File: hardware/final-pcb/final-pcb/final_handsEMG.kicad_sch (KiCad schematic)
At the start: 35 parts, among them J1 Conn_02x13_Odd_Even, U1 ADS1299CPAG

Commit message: finalpcb update (3.23.25)
schematic nearly done, need footprint assignments.
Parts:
- removed D2, D3, D4, D5, D6, D7: TPD4E1B06DRLR, DRL6_TEX, symbol TPD4E1B06DRLR:TPD4E1B06DRLR
- added C29, C31, C33, C37: 10uF, symbol Device:C_Small
- added C30: 0.01uF, symbol Device:C_Small
- added C32, C35, C36, C38, C39, C40: 2.2uF, symbol Device:C_Small
- added D2, D3, D4, D5, D6, D8: TPD4E1B06DCKR, DCK6_TEX, symbol TPD4E1B06DCKR:TPD4E1B06DCKR
- added D9: D_Small, symbol Device:D_Small
- added J2: Conn_01x02, symbol Connector_Generic:Conn_01x02
- added U2: STM32L496ZGT6, STM32L496ZGT6:QFP50P2200X2200X160-144N, symbol STM32L496ZGT6:STM32L496ZGT6
- added U3: LM2664M6/NOPB, DBV0006A_N, symbol LM2664M6/NOPB:LM2664M6_NOPB
- added U4: TLV70025QDDCRQ1, TLV70025QDDCRQ1:SOT95P280X110-5N, symbol TLV70025QDDCRQ1:TLV70025QDDCRQ1
- added U5: MCP1754T-3302E/OT, SOT-23-5_MC_MCH, symbol MCP1754T-3302E/OT:MCP1754T-3302E_OT
- added U6: TPS72325DBVR, TPS72325DBVR:SOT95P280X145-5N, symbol TPS72325DBVR:TPS72325DBVR
- added sC38, sC39, sC43, sC44, sC45, sC46, sC47, sC48, sC55, sC62, sC63, sC65, sC68, sC71: 100nF, symbol Device:C_Small
- added sC64: 1uF_X5R_0603, symbol Device:C_Small
- added sC66, sC69: 4.7uF_X54_0603, symbol Device:C_Small
- added sC67, sC70: 1uF, symbol Device:C_Polarized_Small
- added sC72: 4.7uF, symbol Device:C_Polarized_Small
- added sCN3: USB_B_Micro, symbol Connector:USB_B_Micro
- added sD4: ESDALC6V1_1U2, symbol Device:D_Small
- added sL2: FerriteBead_Small, symbol Device:FerriteBead_Small
- added sLD14: Red, symbol Device:D_Small
- added sLD15: Green, symbol Device:D_Small
- added sR18, sR19, sR9: 10K, symbol Device:R_Small
- added sR21, sR23: 47K, symbol Device:R_Small
- added sR22: 620, symbol Device:R_Small
- added sR24: 22K, symbol Device:R_Small
- added sR25: 330, symbol Device:R_Small
- added sT3: 9013, symbol Transistor_BJT:Q_NPN_BEC
- added sU10: USBLC6-2SC6, Package_TO_SOT_SMD:SOT-23-6, symbol Power_Protection:USBLC6-2SC6
- added sU14: STMPS2151STR, SOT23-5L_STM, symbol STMPS2151STR:STMPS2151STR
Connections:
- net 1N: now also D3.4 (IO3)
- net 1P: now also D2.1 (IO1)
- net 2N: now also D3.2 (IO2)
- net 2P: now also D3.5 (IO4)
- net 3N: now also D4.4 (IO3)
- net 3P: now also D3.1 (IO1)
- net 4N: now also D4.2 (IO2)
- net 4P: now also D4.5 (IO4)
- net 5N: now also D5.4 (IO3)
- net 5P: now also D4.1 (IO1)
- net 6N: now also D5.2 (IO2)
- net 6P: now also D5.5 (IO4)
- net 7N: now also D6.4 (IO3)
- net 7P: now also D5.1 (IO1)
- net 8N: now also D6.2 (IO2)
- net 8P: now also D6.5 (IO4)
- net BIAS: now also D8.4 (IO3)
- net GNDA: now also C29.2, C30.2, C32.2, C33.2, C35.2, C36.2, C37.2, C38.2, C39.2, C40.2, D2.3 (GND), D3.3 (GND), D4.3 (GND), D5.3 (GND), D6.3 (GND), D8.1 (IO1), D8.3 (GND), J2.1 (Pin_1), U2.30 (VSSA/VREF-), U2.31 (VREF-), U3.1 (GND), U4.2 (GND), U5.2 (GND), U6.1 (GND), sC67.2, sC68.2
- net SRB1: now also D2.5 (IO4)
- net SRB2: now also D2.2 (IO2)
- net AVDD renamed +2V5
- net +2V5: now also C35.1, C37.1, D8.2 (IO2), U2.32 (VREF+), U2.33 (VDDA), U4.5 (OUT), sC67.1, sC68.1, sC70.1, sC71.1, sL2.2
- net AVSS renamed -2V5
- net -2V5: now also C29.1, C32.1, D2.4 (IO3), U6.5 (OUT)
- net DVDD renamed +3V3
- net +3V3: now also C38.1, C40.1, U2.106 (VDDUSB), U2.108 (VDD__6), U2.121 (VDD__7), U2.131 (VDDIO2__1), U2.144 (VDD__8), U2.17 (VDD), U2.39 (VDD__1), U2.52 (VDD__2), U2.62 (VDD__3), U2.72 (VDD__4), U2.84 (VDD__5), U2.95 (VDDIO2), U3.4 (SD_N), U3.5 (V+), U4.1 (IN), U4.3 (EN), U5.5 (VOUT), sC38.1, sC39.1, sC43.1, sC44.1, sC45.1, sC46.1, sC47.1, sC48.1, sC55.1, sC62.1, sC63.1, sC64.1, sC65.1, sC66.1, sC69.1, sL2.1, sR21.2, sR22.2, sR25.2, sU14.5 (IN)
- new net: D9.2 (A), J2.2 (Pin_2)
- new net: sC70.2, sC71.2
- new net: sLD14.1 (K), sR21.1, sU14.3 (FAULT)
- new net: sLD14.2 (A), sR22.1
- new net: C30.1, U6.4 (NR)
- new net: U2.138 (PH3-BOOT0), sR9.1
- new net: sLD15.1 (K), sT3.3 (C)
- new net: sLD15.2 (A), sR25.1
- new net: sR23.1, sR24.2, sT3.1 (B)
- new net: sR19.1, sU14.4 (EN)
- new net: C31.1, U3.6 (OUT)
- new net: C31.2, U3.3 (CAP-)
- new net -RAW: C33.1, C36.1, U3.6 (OUT), U6.2 (IN), U6.3 (EN)
- new net 3V Enable: U5.3 (*SHDN)
- new net GND: U2.107 (VSS__7), U2.120 (VSS__8), U2.130 (VSS__9), U2.143 (VSS__10), U2.16 (VSS), U2.38 (VSS__1), U2.51 (VSS__2), U2.61 (VSS__3), U2.71 (VSS__4), U2.83 (VSS__5), U2.94 (VSS__6), sC38.2, sC39.2, sC43.2, sC44.2, sC45.2, sC46.2, sC47.2, sC48.2, sC55.2, sC62.2, sC63.2, sC64.2, sC65.2, sC66.2, sC69.2, sC72.2, sCN3.5 (GND), sD4.2 (A), sR19.2, sR24.1, sR9.2, sT3.2 (E), sU10.2 (GND), sU14.2 (GND)
- new net PA1: U2.35 (PA1)
- new net PA10: U2.102 (PA10), sCN3.4 (ID), sD4.1 (K)
- new net PA11: U2.103 (PA11), sCN3.2 (D-), sU10.3 (I/O2), sU10.4 (I/O2)
- new net PA12: U2.104 (PA12), sCN3.3 (D+), sU10.1 (I/O1), sU10.6 (I/O1)
- new net PA13: U2.105 (PA13(JTMS/SWDIO))
- new net PA14: U2.109 (PA14(JTCK/SWCLK))
- new net PA4: U2.40 (PA4)
- new net PA6: U2.42 (PA6)
- new net PA7: U2.43 (PA7)
- new net PA8: U2.100 (PA8)
- new net PA9: U2.101 (PA9), sR18.1
- new net PB12: U2.73 (PB12)
- new net PB13: U2.74 (PB13)
- new net PB14: U2.75 (PB14)
- new net PB15: U2.76 (PB15)
- new net PB3: U2.133 (PB3(JTDO/TRACESWO))
- new net PB7: U2.137 (PB7)
- new net PC13: U2.7 (PC13)
- new net PC7: U2.97 (PC7)
- new net PD10: U2.79 (PD10)
- new net PD11: U2.80 (PD11)
- new net PD12: U2.81 (PD12)
- new net PD13: U2.82 (PD13)
- new net PD8: U2.77 (PD8)
- new net PD9: U2.78 (PD9)
- new net PG13: U2.128 (PG13)
- new net PG14: U2.129 (PG14)
- new net RAW: C39.1, D9.1 (K), U5.1 (VIN)
- new net USB_VBUS: sC72.1, sCN3.1 (VBUS), sR18.2, sR23.2, sU10.5 (VBUS), sU14.1 (OUT)
- new net VBAT: U2.6 (VBAT)
- new net /NRST: U2.25 (~{NRST})
- no-connect marks 2 -> 91
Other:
- removed sheet FinalPCB_STM32
- moved on the sheet: C1, C11, C12, C13, C14, C15, C17, C18, C19, C2, C21, C22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

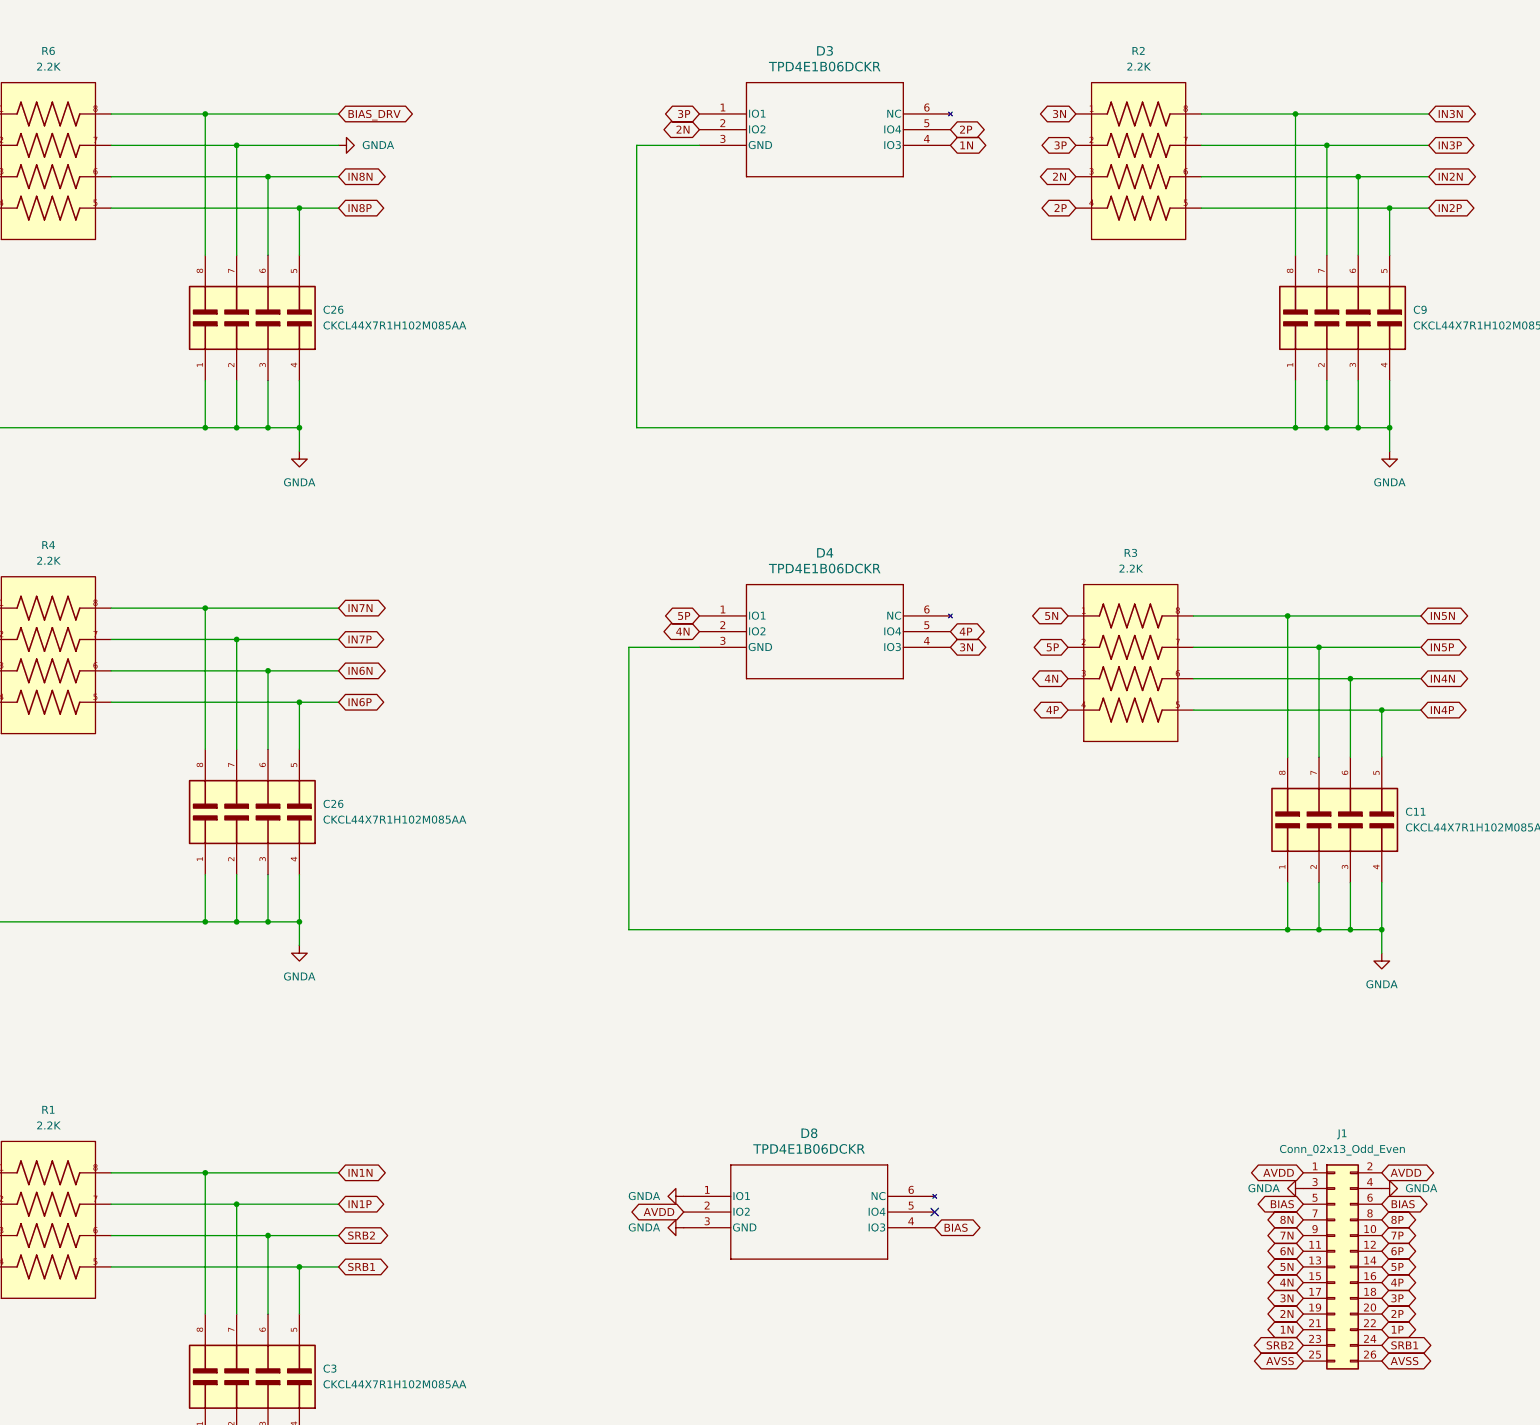
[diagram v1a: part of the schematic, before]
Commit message: half ads layout done (3.24.25)
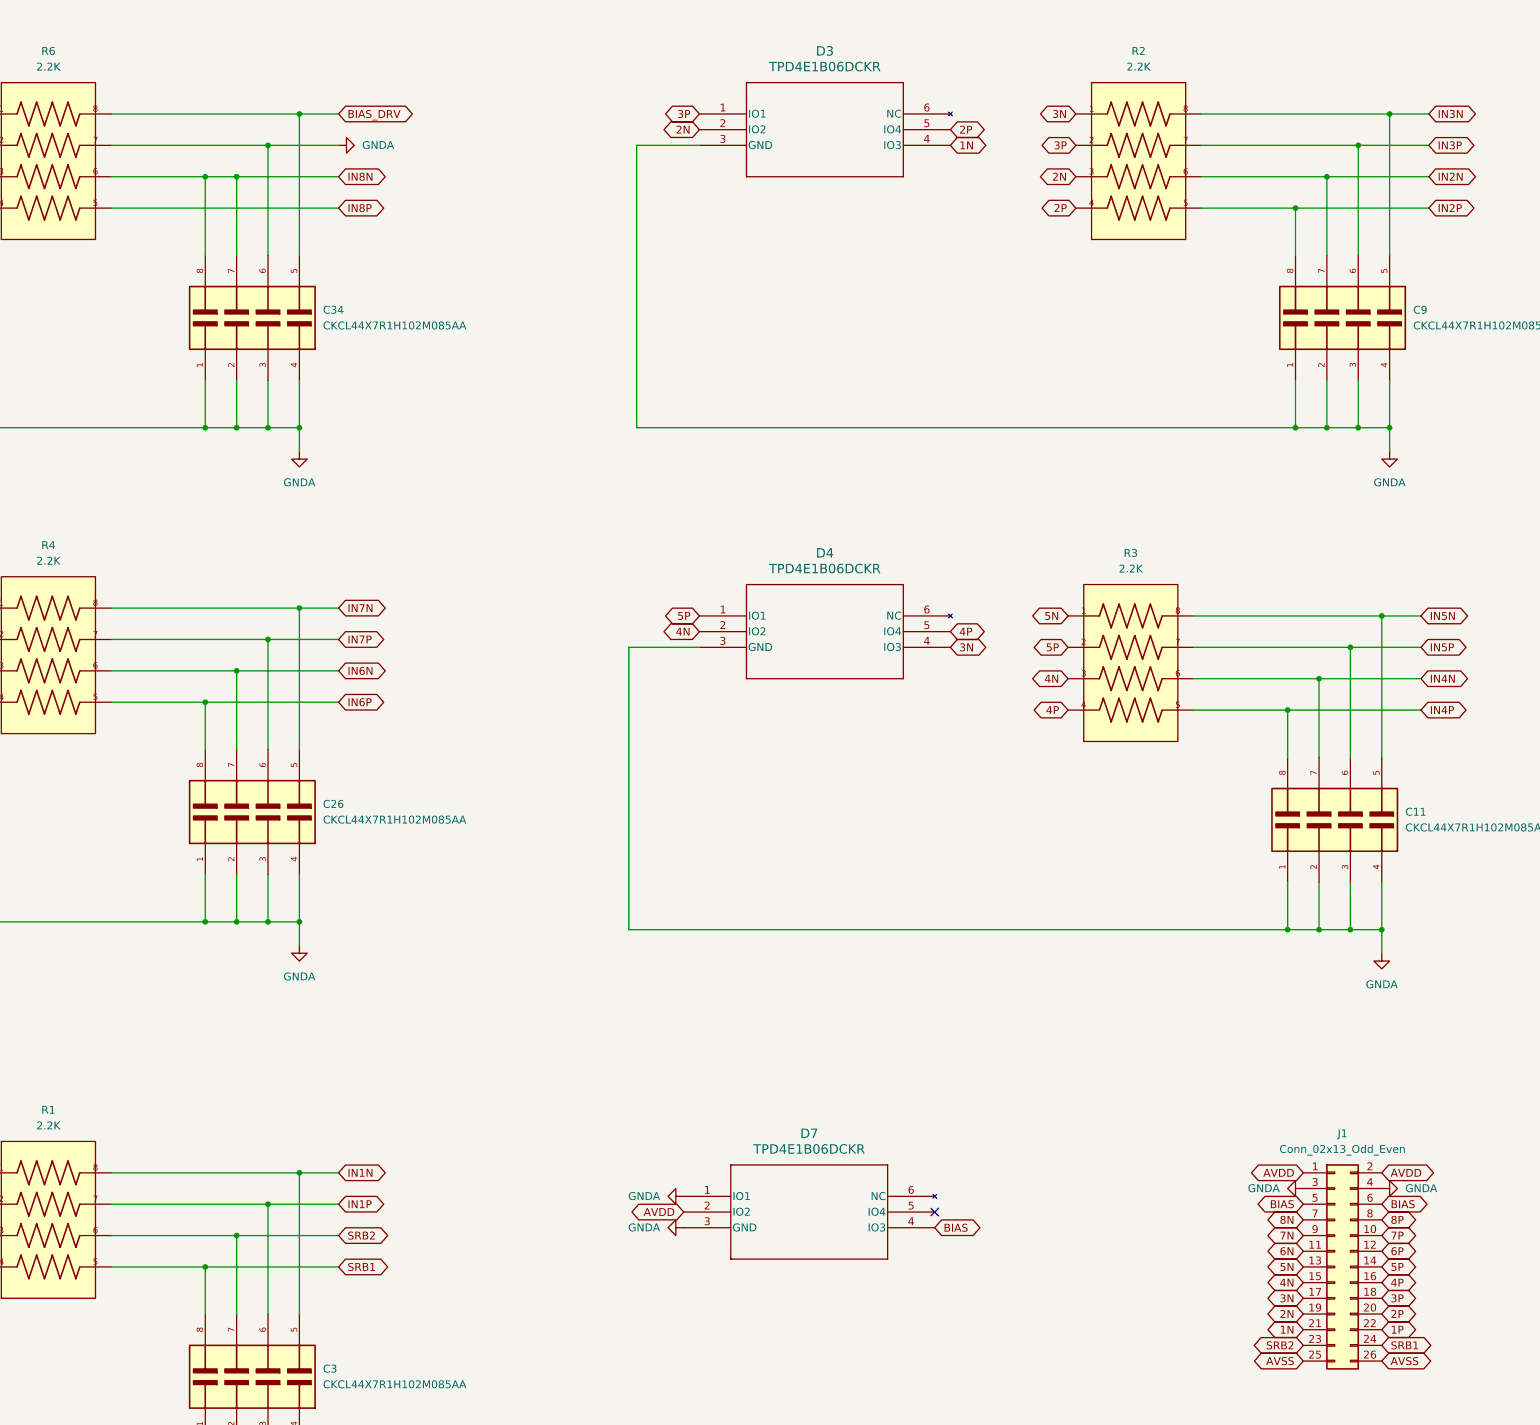
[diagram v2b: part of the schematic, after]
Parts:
- C1, C29, C31, C33, C37: footprint (none) -> GRM188C80G106KE47D:CAPC1608X90N
- C12, C13, C15, C24, C28, C5: footprint (none) -> CC0402KRX7R7BB104:YAG_CC0402_YAG
- C14, C17, C18, C19, C21, C22, C27, C6, C7: footprint (none) -> CC0402KRX7R5BB105:CAP_CC0402KRX7R5BB105_YAG
- C2: footprint (none) -> CC1206MKX5R5BB107:CAP_CC1206_YAG
- C30: footprint (none) -> CC0402KRX7R7BB103:CC0402N_YAG
- C32, C35, C36, C38, C40: footprint (none) -> GRM155C80J225ME95D:CAPC1005X55N
- C39: footprint (none) -> GRM155R61C225KE44D:CAP_GRM155R61C225KE44D_MUR
- D2, D3, D4, D5, D6: footprint DCK6_TEX -> TPD4E1B06DCKR:DCK6_TEX
- D7: renamed from D8; footprint DCK6_TEX -> TPD4E1B06DCKR:DCK6_TEX
- J1: footprint (none) -> 68021_226HLF:AMPHENOL_68021-226HLF
- R1, R2, R3, R4, R6: footprint CAY16-222J4LF:RESCAF80P320X160X60-8N -> CAY16-2201F4LF:CAY16_BRN
- U3: footprint DBV0006A_N -> (none)
- U5: footprint SOT-23-5_MC_MCH -> (none)
- sU14: footprint SOT23-5L_STM -> (none)
- renumbered C26 to C34
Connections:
- net BIAS_DRV: now also C34.5; no longer C34.8
- net GNDA: now also C34.6; no longer C34.7
- net IN1N: now also C3.5; no longer C3.8
- net IN1P: now also C3.6; no longer C3.7
- net IN2N: now also C9.7; no longer C9.6
- net IN2P: now also C9.8; no longer C9.5
- net IN3N: now also C9.5; no longer C9.8
- net IN3P: now also C9.6; no longer C9.7
- net IN4N: now also C11.7; no longer C11.6
- net IN4P: now also C11.8; no longer C11.5
- net IN5N: now also C11.5; no longer C11.8
- net IN5P: now also C11.6; no longer C11.7
- net IN6N: now also C26.7; no longer C26.6
- net IN6P: now also C26.8; no longer C26.5
- net IN7N: now also C26.5; no longer C26.8
- net IN7P: now also C26.6; no longer C26.7
- net IN8N: now also C34.7, C34.8; no longer C34.6
- net IN8P: no longer C34.5
- net SRB1: now also C3.8; no longer C3.5
- net SRB2: now also C3.7; no longer C3.6

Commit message: added stm32 decoupling circuitry and usb (3.24.25)
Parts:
- renumbered sC48 to sC28, sC45 to sC29, sC44 to sC30, sC62 to sC31, sC46 to sC32, sC38 to sC33, sC55 to sC34, sC72 to sC42, sC43 to sC49, sC63 to sC50, sC65 to sC51, sC69 to sC52, sC39 to sC53, sC66 to sC54, sC70 to sC56, sC71 to sC57, sC68 to sC58, sC67 to sC59, sC64 to sC60, sC47 to sC61, sCN3 to sCN14, sD4 to sD6, sL2 to sL3, sLD14 to sLD7, sLD15 to sLD8, sR9 to sR38, sR25 to sR41, sR22 to sR45, sR24 to sR48, sR23 to sR49, sR21 to sR51, sR19 to sR52, sR18 to sR54, sT3 to sT2, sU14 to sU12, sU10 to sU13
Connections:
- net GNDA: now also sC56.2, sC57.2
- net PA11: now also sU13.1 (I/O1), sU13.6 (I/O1); no longer sU13.3 (I/O2), sU13.4 (I/O2)
- net PA12: now also sU13.3 (I/O2), sU13.4 (I/O2); no longer sU13.1 (I/O1), sU13.6 (I/O1)

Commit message: basic routing (3.30.25)
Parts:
- added sD10: ESDALC6V1W5, ESDALC6V1W5:SOT65P210X110-5N, symbol ESDALC6V1W5:ESDALC6V1W5
- added sJ3: FTSH-107-01-L-DV-K, FTSH_107_01_L_DV_K:CON14_2X7_DUK_FTSH_SAI, symbol FTSH-107-01-L-DV-K:FTSH-107-01-L-DV-K
- sC28, sC29, sC30, sC31, sC32, sC33, sC34, sC49, sC50, sC51, sC53, sC57, sC58, sC61: footprint (none) -> CC0603KRX7R7BB104:CAPC1608X90
- sC42: footprint (none) -> TAJA475K016R:CAPMP3216X166
- sC52, sC54: footprint (none) -> CC0603KRX5R7BB475:CAPC1608X90
- sC56, sC59: footprint (none) -> TAJA105K016R:CAPMP3216X166
- sC60: footprint (none) -> CC0603KRX5R7BB105:CAPC1608X90
- sCN14: footprint (none) -> 47589-1001:MOLEX_47589-1001
- sD6: footprint (none) -> ESDALC6V1-1U2:DIODE_ESDALC6V1-1U2
- sL3: footprint (none) -> FCM1608KF-601T05:FB0603
- sLD7: footprint (none) -> LED-SMD-RED-DIFFUSED_0603_:LED-0603
- sLD8: footprint (none) -> SMD-LED-CLEAR-GREEN_0603_:LED-0603
- sR38, sR52, sR54: footprint (none) -> RC0603FR-0710KL:RESC1607X60N
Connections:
- net +3V3: now also sJ3.3
- net GND: now also sD10.2 (GND), sJ3.5, sJ3.7
- net IN8N: no longer C34.8
- net IN8P: now also C34.8
- net PA13: now also sD10.4 (I/03), sJ3.4
- net PA14: now also sD10.5 (I/04), sJ3.6
- net PB3: now also sD10.1 (I/01), sJ3.8
- net /NRST renamed NRST
- net NRST: now also sD10.3 (I/02), sJ3.12
- no-connect marks 91 -> 98
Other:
- moved on the sheet: U2, sC28, sC29, sC30, sC31, sC32, sC33, sC34, sC42, sC49, sC50, sC51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
